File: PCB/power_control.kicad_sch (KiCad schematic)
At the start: 10 parts

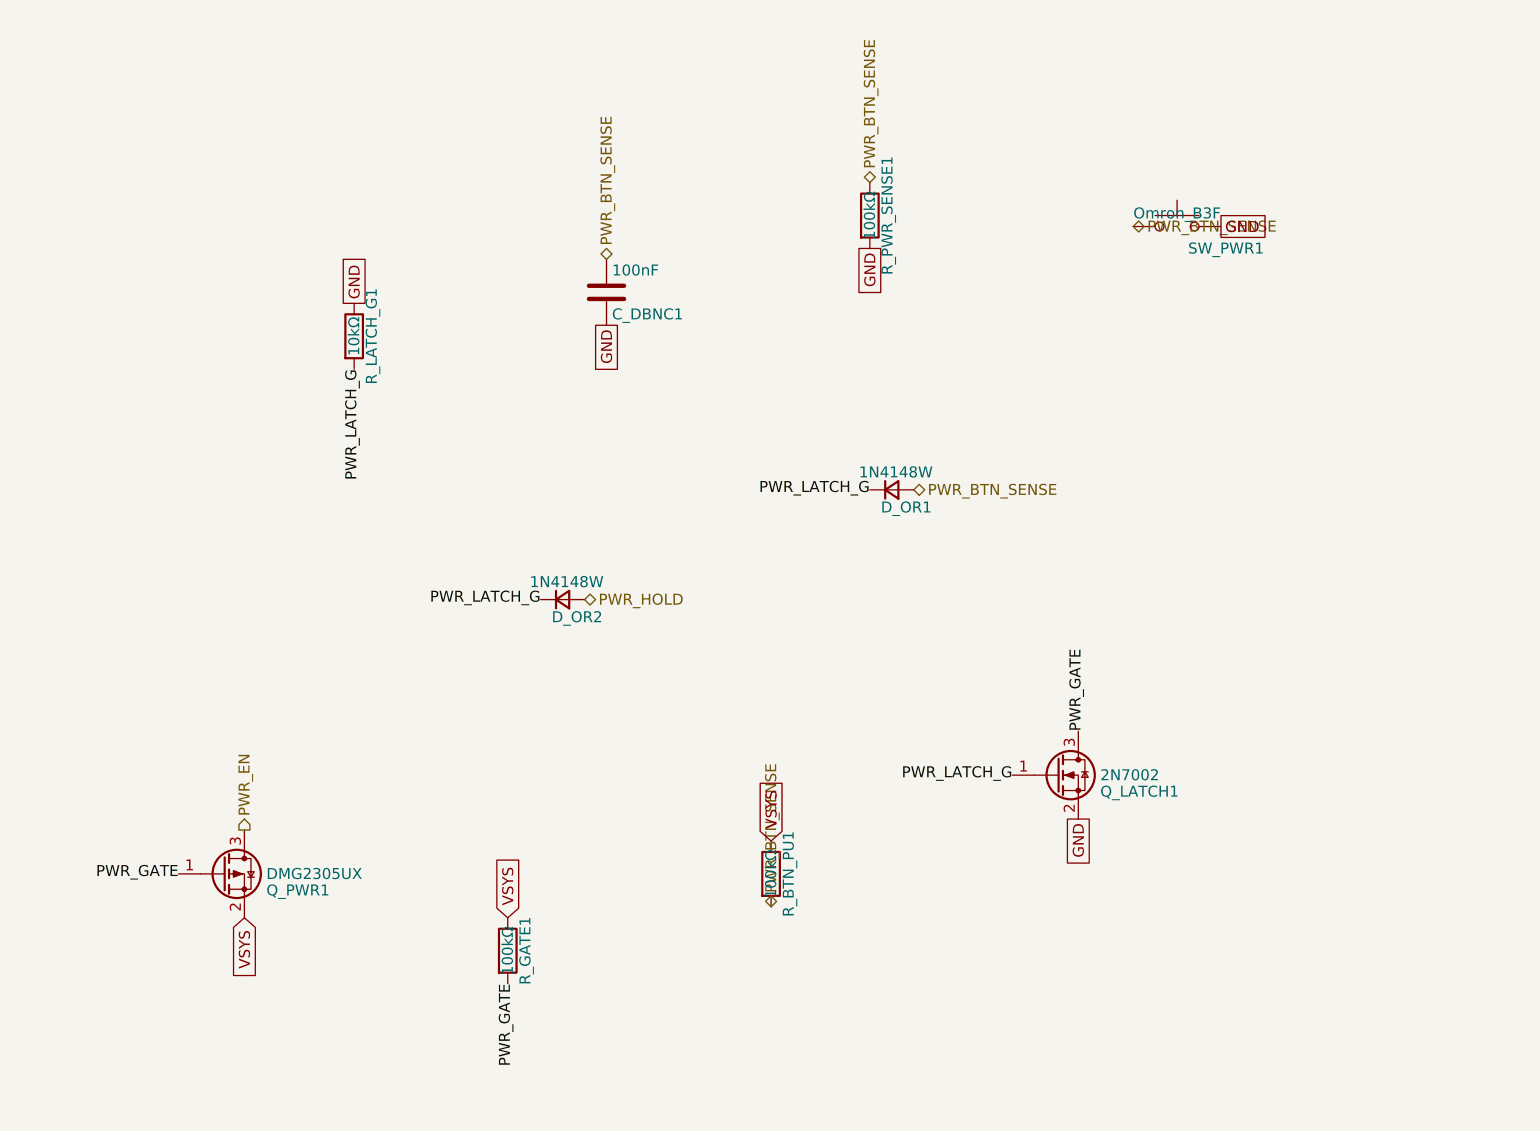
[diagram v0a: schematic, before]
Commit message: refactor: updated gulikit footprint
This updates the gulikit thumbstick footprint to be accurate.
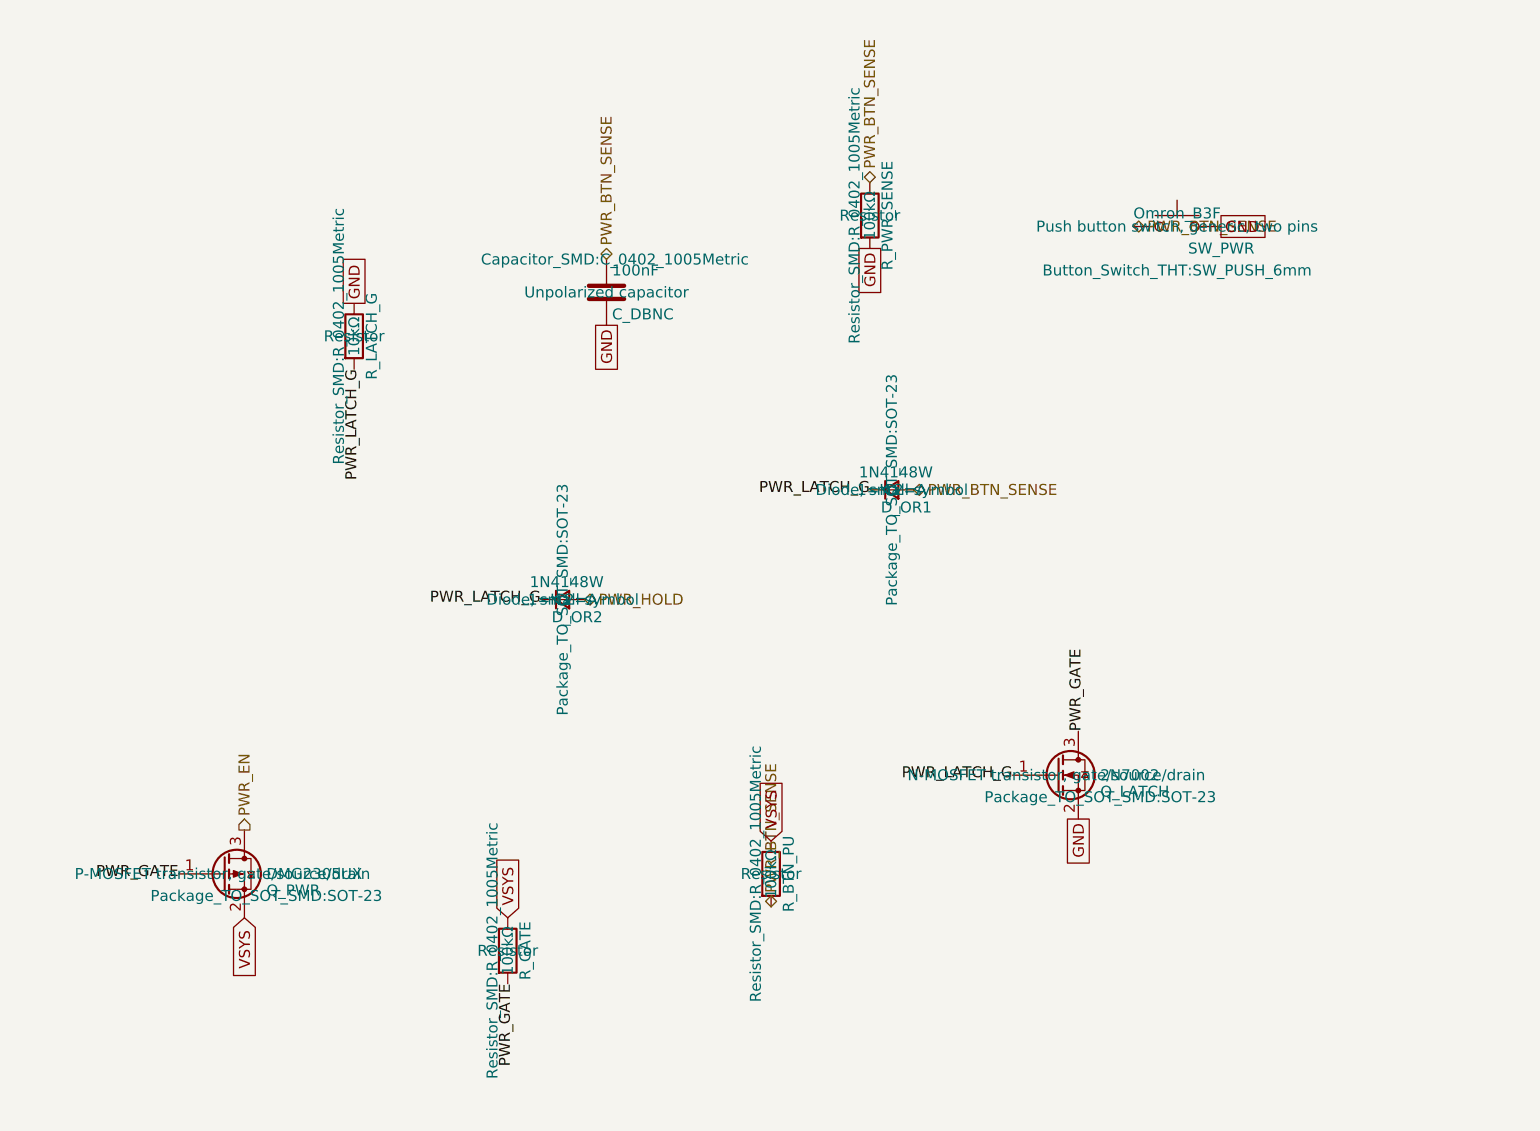
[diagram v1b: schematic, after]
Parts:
- removed C_DBNC1: 100nF, Capacitor_SMD:C_0402_1005Metric, symbol Device:C
- removed Q_LATCH1: 2N7002, Package_TO_SOT_SMD:SOT-23, symbol Transistor_FET:Q_NMOS_GSD
- removed Q_PWR1: DMG2305UX, Package_TO_SOT_SMD:SOT-23, symbol Transistor_FET:Q_PMOS_GSD
- removed R_BTN_PU1, R_GATE1, R_PWR_SENSE1: 100kΩ, Resistor_SMD:R_0402_1005Metric, symbol Device:R
- removed R_LATCH_G1: 10kΩ, Resistor_SMD:R_0402_1005Metric, symbol Device:R
- removed SW_PWR1: Omron_B3F, Button_Switch_THT:SW_PUSH_6mm, symbol Switch:SW_Push
- added C_DBNC: 100nF, Capacitor_SMD:C_0402_1005Metric, symbol Device:C
- added Q_LATCH: 2N7002, Package_TO_SOT_SMD:SOT-23, symbol Transistor_FET:Q_NMOS_GSD
- added Q_PWR: DMG2305UX, Package_TO_SOT_SMD:SOT-23, symbol Transistor_FET:Q_PMOS_GSD
- added R_BTN_PU, R_GATE, R_PWR_SENSE: 100kΩ, Resistor_SMD:R_0402_1005Metric, symbol Device:R
- added R_LATCH_G: 10kΩ, Resistor_SMD:R_0402_1005Metric, symbol Device:R
- added SW_PWR: Omron_B3F, Button_Switch_THT:SW_PUSH_6mm, symbol Switch:SW_Push
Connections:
- net GND: now also C_DBNC.2, Q_LATCH.2 (S), R_LATCH_G.1, R_PWR_SENSE.2, SW_PWR.2
- net PWR_BTN_SENSE: now also C_DBNC.1, R_BTN_PU.2, R_PWR_SENSE.1, SW_PWR.1
- net PWR_EN: now also Q_PWR.3 (D)
- net PWR_GATE: now also Q_LATCH.3 (D), Q_PWR.1 (G), R_GATE.2
- net PWR_LATCH_G: now also Q_LATCH.1 (G), R_LATCH_G.2
- net VSYS: now also Q_PWR.2 (S), R_BTN_PU.1, R_GATE.1

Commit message: layout: beginning pcb layout
This updates the schematic with a few different footprints while also starts the layout.
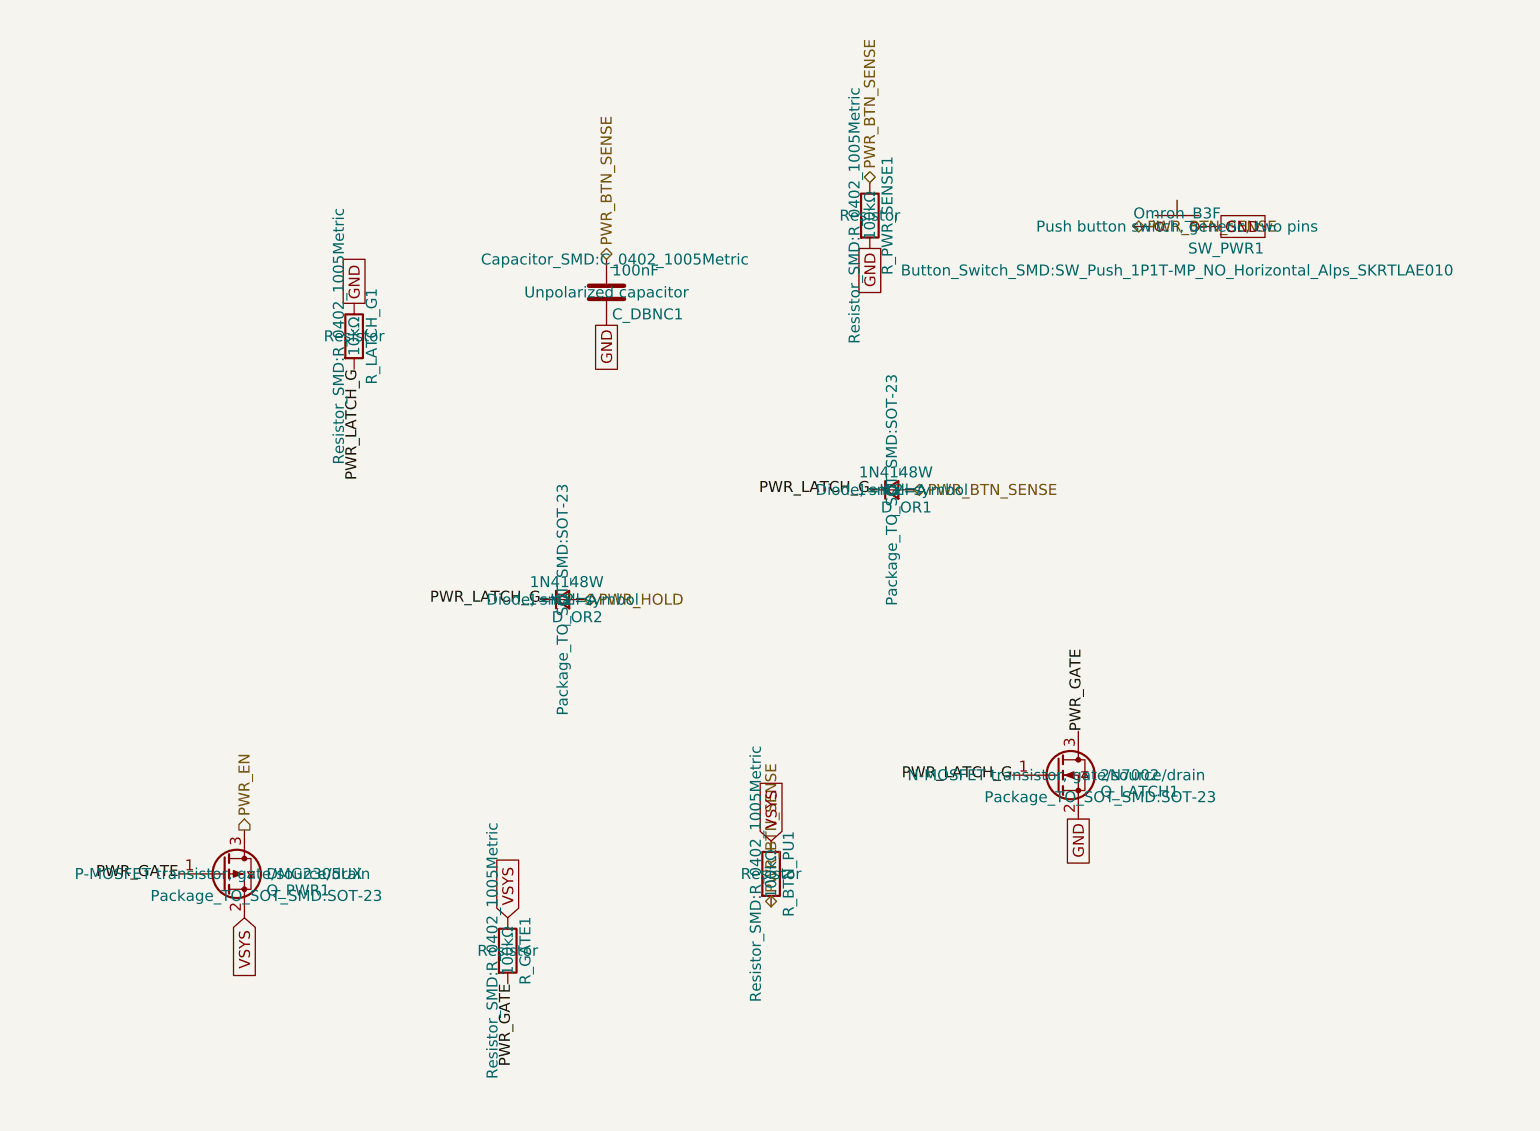
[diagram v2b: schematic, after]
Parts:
- SW_PWR1: renamed from SW_PWR; footprint Button_Switch_THT:SW_PUSH_6mm -> Button_Switch_SMD:SW_Push_1P1T-MP_NO_Horizontal_Alps_SKRTLAE010
- renumbered C_DBNC to C_DBNC1, Q_LATCH to Q_LATCH1, Q_PWR to Q_PWR1, R_BTN_PU to R_BTN_PU1, R_GATE to R_GATE1, R_LATCH_G to R_LATCH_G1, R_PWR_SENSE to R_PWR_SENSE1
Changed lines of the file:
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@@
 		)
 		(instances
+			(project "snips_controller"
+				(path "/868f8289-8434-4465-b2f4-2accc5e40bab/c56f3d5f-543a-4bd1-90c4-022a9c6f97c6"
+					(reference "D_OR2")
+					(unit 1)
+				)
+			)
 			(project ""
 				(path "/d0f5b7d7-b2b6-4492-958c-e60265d3c6b4/c56f3d5f-543a-4bd1-90c4-022a9c6f97c6"
@@
 		(dnp no)
 		(fields_autoplaced yes)
-		(property "Reference" "R_LATCH_G"
+		(property "Reference" "R_LATCH_G1"
 			(at 109.982 76.2 90)
 			(show_name no)
@@
 		)
 		(instances
+			(project "snips_controller"
+				(path "/868f8289-8434-4465-b2f4-2accc5e40bab/c56f3d5f-543a-4bd1-90c4-022a9c6f97c6"
+					(reference "R_LATCH_G1")
+					(unit 1)
+				)
+			)
 			(project ""
 				(path "/d0f5b7d7-b2b6-4492-958c-e60265d3c6b4/c56f3d5f-543a-4bd1-90c4-022a9c6f97c6"
@@
 		(dnp no)
 		(fields_autoplaced yes)
-		(property "Reference" "C_DBNC"
+		(property "Reference" "C_DBNC1"
 			(at 137.795 73.66 0)
 			(show_name no)
@@
 		)
 		(instances
+			(project "snips_controller"
+				(path "/868f8289-8434-4465-b2f4-2accc5e40bab/c56f3d5f-543a-4bd1-90c4-022a9c6f97c6"
+					(reference "C_DBNC1")
+					(unit 1)
+				)
+			)
 			(project ""
 				(path "/d0f5b7d7-b2b6-4492-958c-e60265d3c6b4/c56f3d5f-543a-4bd1-90c4-022a9c6f97c6"
@@
 		(dnp no)
 		(fields_autoplaced yes)
-		(property "Reference" "R_PWR_SENSE"
+		(property "Reference" "R_PWR_SENSE1"
 			(at 169.672 62.23 90)
 			(show_name no)
@@
 		)
 		(instances
+			(project "snips_controller"
+				(path "/868f8289-8434-4465-b2f4-2accc5e40bab/c56f3d5f-543a-4bd1-90c4-022a9c6f97c6"
+					(reference "R_PWR_SENSE1")
+					(unit 1)
+				)
+			)
 			(project ""
 				(path "/d0f5b7d7-b2b6-4492-958c-e60265d3c6b4/c56f3d5f-543a-4bd1-90c4-022a9c6f97c6"
@@
 		(dnp no)
 		(fields_autoplaced yes)
-		(property "Reference" "Q_PWR"
+		(property "Reference" "Q_PWR1"
 			(at 97.79 140.335 0)
 			(show_name no)
@@
 		)
 		(instances
+			(project "snips_controller"
+				(path "/868f8289-8434-4465-b2f4-2accc5e40bab/c56f3d5f-543a-4bd1-90c4-022a9c6f97c6"
+					(reference "Q_PWR1")
+					(unit 1)
+				)
+			)
 			(project ""
 				(path "/d0f5b7d7-b2b6-4492-958c-e60265d3c6b4/c56f3d5f-543a-4bd1-90c4-022a9c6f97c6"
@@
 		(dnp no)
 		(fields_autoplaced yes)
-		(property "Reference" "R_GATE"
+		(property "Reference" "R_GATE1"
 			(at 127.762 147.32 90)
 			(show_name no)
@@
 		)
 		(instances
+			(project "snips_controller"
+				(path "/868f8289-8434-4465-b2f4-2accc5e40bab/c56f3d5f-543a-4bd1-90c4-022a9c6f97c6"
+					(reference "R_GATE1")
+					(unit 1)
+				)
+			)
 			(project ""
 				(path "/d0f5b7d7-b2b6-4492-958c-e60265d3c6b4/c56f3d5f-543a-4bd1-90c4-022a9c6f97c6"
@@
 		(dnp no)
 		(fields_autoplaced yes)
-		(property "Reference" "SW_PWR"
+		(property "Reference" "SW_PWR1"
 			(at 204.47 66.04 0)
 			(show_name no)
@@
 			)
 		)
-		(property "Footprint" "Button_Switch_THT:SW_PUSH_6mm"
+		(property "Footprint" "Button_Switch_SMD:SW_Push_1P1T-MP_NO_Horizontal_Alps_SKRTLAE010"
 			(at 203.2 68.58 0)
 			(show_name no)
@@
 		)
 		(instances
+			(project "snips_controller"
+				(path "/868f8289-8434-4465-b2f4-2accc5e40bab/c56f3d5f-543a-4bd1-90c4-022a9c6f97c6"
+					(reference "SW_PWR1")
+					(unit 1)
+				)
+			)
 			(project ""
 				(path "/d0f5b7d7-b2b6-4492-958c-e60265d3c6b4/c56f3d5f-543a-4bd1-90c4-022a9c6f97c6"
@@
 		(dnp no)
 		(fields_autoplaced yes)
-		(property "Reference" "Q_LATCH"
+		(property "Reference" "Q_LATCH1"
 			(at 194.31 128.905 0)
 			(show_name no)
@@
 		)
 		(instances
+			(project "snips_controller"
+				(path "/868f8289-8434-4465-b2f4-2accc5e40bab/c56f3d5f-543a-4bd1-90c4-022a9c6f97c6"
+					(reference "Q_LATCH1")
+					(unit 1)
+				)
+			)
 			(project ""
 				(path "/d0f5b7d7-b2b6-4492-958c-e60265d3c6b4/c56f3d5f-543a-4bd1-90c4-022a9c6f97c6"
@@
 		(dnp no)
 		(fields_autoplaced yes)
-		(property "Reference" "R_BTN_PU"
+		(property "Reference" "R_BTN_PU1"
 			(at 158.242 138.43 90)
 			(show_name no)
@@
 		)
 		(instances
+			(project "snips_controller"
+				(path "/868f8289-8434-4465-b2f4-2accc5e40bab/c56f3d5f-543a-4bd1-90c4-022a9c6f97c6"
+					(reference "R_BTN_PU1")
+					(unit 1)
+				)
+			)
 			(project ""
 				(path "/d0f5b7d7-b2b6-4492-958c-e60265d3c6b4/c56f3d5f-543a-4bd1-90c4-022a9c6f97c6"
@@
 		)
 		(instances
-			(project ""
-				(path "/d0f5b7d7-b2b6-4492-958c-e60265d3c6b4/c56f3d5f-543a-4bd1-90c4-022a9c6f97c6"
+			(project "snips_controller"
+				(path "/868f8289-8434-4465-b2f4-2accc5e40bab/c56f3d5f-543a-4bd1-90c4-022a9c6f97c6"
+					(reference "D_OR1")
+					(unit 1)
+				)
+			)
+			(project ""
+				(path "/d0f5b7d7-b2b6-4492-958c-e60265d3c6b4/c56f3d5f-543a-4bd1-90c4-022a9c6f97c6"

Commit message: refactor: swap footprints and add symmetry
This updates the footprints of a couple components to be smaller and closer to what we want. It also adds two buttons to ensure left and right side symmetry.
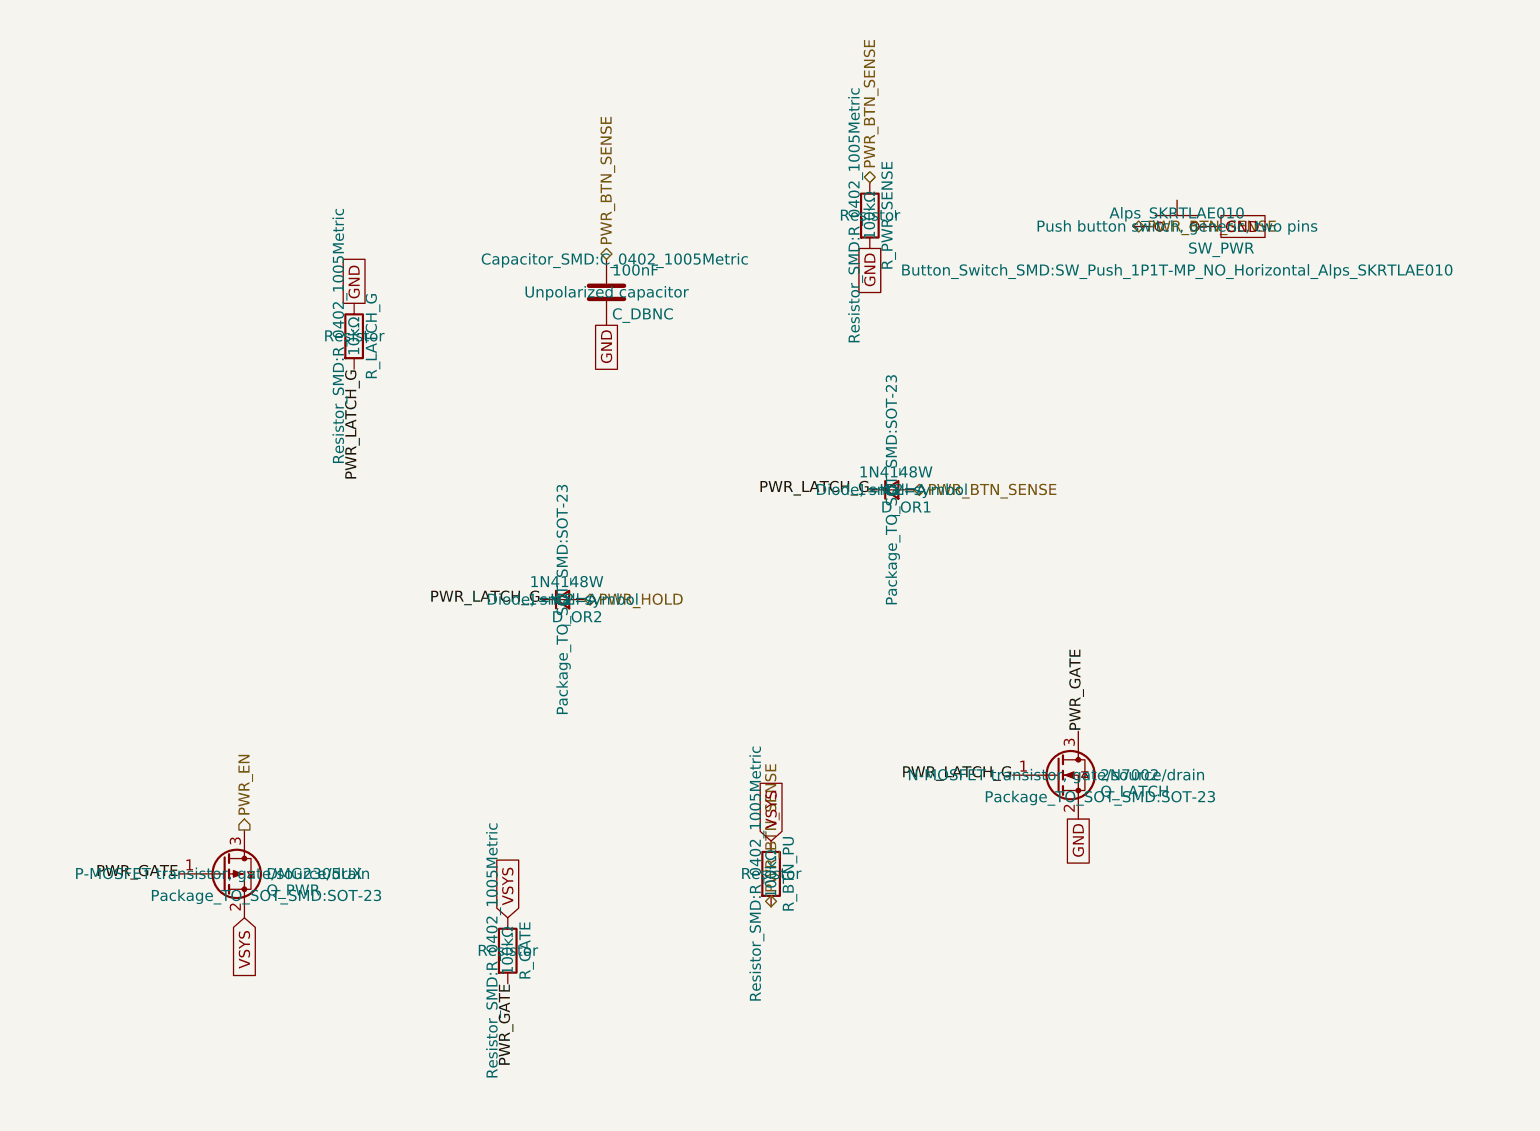
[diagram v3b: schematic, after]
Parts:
- removed C_DBNC1: 100nF, Capacitor_SMD:C_0402_1005Metric, symbol Device:C
- removed Q_LATCH1: 2N7002, Package_TO_SOT_SMD:SOT-23, symbol Transistor_FET:Q_NMOS_GSD
- removed Q_PWR1: DMG2305UX, Package_TO_SOT_SMD:SOT-23, symbol Transistor_FET:Q_PMOS_GSD
- removed R_BTN_PU1, R_GATE1, R_PWR_SENSE1: 100kΩ, Resistor_SMD:R_0402_1005Metric, symbol Device:R
- removed R_LATCH_G1: 10kΩ, Resistor_SMD:R_0402_1005Metric, symbol Device:R
- removed SW_PWR1: Omron_B3F, Button_Switch_SMD:SW_Push_1P1T-MP_NO_Horizontal_Alps_SKRTLAE010, symbol Switch:SW_Push
- added C_DBNC: 100nF, Capacitor_SMD:C_0402_1005Metric, symbol Device:C
- added Q_LATCH: 2N7002, Package_TO_SOT_SMD:SOT-23, symbol Transistor_FET:Q_NMOS_GSD
- added Q_PWR: DMG2305UX, Package_TO_SOT_SMD:SOT-23, symbol Transistor_FET:Q_PMOS_GSD
- added R_BTN_PU, R_GATE, R_PWR_SENSE: 100kΩ, Resistor_SMD:R_0402_1005Metric, symbol Device:R
- added R_LATCH_G: 10kΩ, Resistor_SMD:R_0402_1005Metric, symbol Device:R
- added SW_PWR: Alps_SKRTLAE010, Button_Switch_SMD:SW_Push_1P1T-MP_NO_Horizontal_Alps_SKRTLAE010, symbol Switch:SW_Push
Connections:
- net GND: now also C_DBNC.2, Q_LATCH.2 (S), R_LATCH_G.1, R_PWR_SENSE.2, SW_PWR.2
- net PWR_BTN_SENSE: now also C_DBNC.1, R_BTN_PU.2, R_PWR_SENSE.1, SW_PWR.1
- net PWR_EN: now also Q_PWR.3 (D)
- net PWR_GATE: now also Q_LATCH.3 (D), Q_PWR.1 (G), R_GATE.2
- net PWR_LATCH_G: now also Q_LATCH.1 (G), R_LATCH_G.2
- net VSYS: now also Q_PWR.2 (S), R_BTN_PU.1, R_GATE.1
